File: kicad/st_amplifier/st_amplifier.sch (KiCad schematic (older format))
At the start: 67 parts

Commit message: He completed the first version of the board st_amplifier.
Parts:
- R1: value 2 к +/-0.5% -> 2 к +/-0.5%
- R2: value 28.7 к +/-0.5% -> 28.7 к +/-0.5%
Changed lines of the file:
@@
 Sheet 1 1
 Title ""
-Date "22 may 2015"
+Date "27 may 2015"
 Rev ""
 Comp ""
@@
 P 9300 3100
 F 0 "R1" H 9450 3350 71  0000 C CNN
-F 1 "2 к  +/-0.5%" H 9450 3250 71  0000 C CNN
+F 1 "2 к +/-0.5%" H 9450 3250 71  0000 C CNN
 F 2 "" H 9300 3100 60  0001 C CNN
 F 3 "" H 9300 3100 60  0001 C CNN
@@
 P 10500 3100
 F 0 "R2" H 10650 3350 71  0000 C CNN
-F 1 "28.7 к  +/-0.5%" H 10650 3250 71  0000 C CNN
+F 1 "28.7 к +/-0.5%" H 10650 3250 71  0000 C CNN
 F 2 "" H 10500 3100 60  0001 C CNN
 F 3 "" H 10500 3100 60  0001 C CNN

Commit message: Adding new version st_amplifier.
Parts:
- added C35, C36: 22 п, symbol CAPITORS
- added R21, R22: 220, symbol RESISTOR
- added R25, R26: 4.7, symbol RESISTOR
- added XP3: WF-3, ~, symbol PIN_M_3
- C12, C13: value 10 п -> 22 п
- C21, C27: value 100 п -> 220 п
- C28, C9: value 0.1 мк -> 0.047 мк
- XP1: renamed from XS2; symbol PIN_F_5 -> PIN_M_5
- XP2: renamed from XS4; value WF-4 -> WF-3; symbol PIN_M_4 -> PIN_M_3
- renumbered XS3 to XS2, XS6 to XS3
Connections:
- wire segments 201 -> 204
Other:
- moved on the sheet: C20, C24, R12, R18, R19, R4

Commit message: New commit.
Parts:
- added C37, C38: 22 п, symbol CAPITORS
- R14, R2: value 28.7 к +/-0.5% -> 28 к +/-0.5%
- R6, R8: value 22.1 к +/-0.5% -> 24 к +/-0.5%
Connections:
- net +29V: now also XP1.1; no longer XP1.2
- net MU/ST: now also XP1.2; no longer XP1.1
- net at DA4.14 (OUT), L1.2, R2.2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: now also C38.2
- net at DA4.2 (~IN), R1.2, R2.1: now also C38.1
- net at DA5.14 (OUT), L2.2, R14.2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: now also C37.2
- net at DA5.2 (~IN), R13.2, R14.1: now also C37.1
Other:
- moved on the sheet: C24, C27, R18, R22, XP3
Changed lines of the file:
@@
 Sheet 1 1
 Title ""
-Date "27 may 2015"
+Date "4 jun 2015"
 Rev ""
 Comp ""
@@
 Wire Wire Line
 	2800 6100 3350 6100
-Wire Wire Line
-	3350 6100 3350 5950
 Connection ~ 2800 6100
 Wire Wire Line
@@
 Connection ~ 12400 5600
 Wire Wire Line
-	9850 3650 9750 3650
-Wire Wire Line
-	9750 3650 9750 3100
+	9750 3650 9850 3650
+Wire Wire Line
+	9750 2700 9750 3650
 Wire Wire Line
 	8800 3200 8800 3100
@@
 	8800 3550 9100 3550
 Wire Wire Line
-	11550 3100 11550 3650
+	11550 2700 11550 3650
 Wire Wire Line
 	9100 3450 9100 3750
@@
 U 1 1 532EE9DE
 P 9300 3100
-F 0 "R1" H 9450 3350 71  0000 C CNN
-F 1 "2 к +/-0.5%" H 9450 3250 71  0000 C CNN
+F 0 "R1" H 9350 3350 71  0000 C CNN
+F 1 "2 к +/-0.5%" H 9350 3250 71  0000 C CNN
 F 2 "" H 9300 3100 60  0001 C CNN
 F 3 "" H 9300 3100 60  0001 C CNN
@@
 P 10500 3100
 F 0 "R2" H 10650 3350 71  0000 C CNN
-F 1 "28.7 к +/-0.5%" H 10650 3250 71  0000 C CNN
+F 1 "28 к +/-0.5%" H 10650 3250 71  0000 C CNN
 F 2 "" H 10500 3100 60  0001 C CNN
 F 3 "" H 10500 3100 60  0001 C CNN
@@
 Connection ~ 12200 9150
 Wire Wire Line
-	9650 7200 9550 7200
-Wire Wire Line
-	9550 7200 9550 6650
+	9550 7200 9650 7200
+Wire Wire Line
+	9550 6200 9550 7200
 Wire Wire Line
 	8600 6750 8600 6650
@@
 	8600 7100 8900 7100
 Wire Wire Line
-	11350 6650 11350 7200
+	11350 6200 11350 7200
 Wire Wire Line
 	8900 7000 8900 7300
@@
 U 1 1 552A86A8
 P 9100 6650
-F 0 "R13" H 9250 6900 71  0000 C CNN
-F 1 "2 к +/-0.5%" H 9250 6800 71  0000 C CNN
+F 0 "R13" H 9150 6900 71  0000 C CNN
+F 1 "2 к +/-0.5%" H 9150 6800 71  0000 C CNN
 F 2 "" H 9100 6650 60  0001 C CNN
 F 3 "" H 9100 6650 60  0001 C CNN
@@
 P 10300 6650
 F 0 "R14" H 10450 6900 71  0000 C CNN
-F 1 "28.7 к +/-0.5%" H 10450 6800 71  0000 C CNN
+F 1 "28 к +/-0.5%" H 10450 6800 71  0000 C CNN
 F 2 "" H 10300 6650 60  0001 C CNN
 F 3 "" H 10300 6650 60  0001 C CNN
@@
 Text Label 6900 1350 2    60   ~ 0
 +15V
-Connection ~ 3350 6700
-Wire Wire Line
-	2550 6700 2950 6700
-Wire Wire Line
-	3200 6700 3850 6700
-Wire Wire Line
-	2800 7100 2800 7550
-Connection ~ 2800 6700
-Wire Wire Line
-	2800 6700 2800 6850
-Wire Wire Line
-	3350 6700 3350 6850
-Wire Wire Line
-	2800 7250 3350 7250
-Wire Wire Line
-	3350 7250 3350 7100
-Connection ~ 2800 7250
-Text Label 2800 7550 1    60   ~ 0
+Connection ~ 3350 6650
+Wire Wire Line
+	2550 6650 2950 6650
+Wire Wire Line
+	3200 6650 3950 6650
+Wire Wire Line
+	2800 7050 2800 7500
+Connection ~ 2800 6650
+Wire Wire Line
+	2800 6650 2800 6800
+Wire Wire Line
+	3350 6650 3350 6800
+Wire Wire Line
+	2800 7200 3350 7200
+Connection ~ 2800 7200
+Text Label 2800 7500 1    60   ~ 0
 GND
 $Comp
 L RESISTOR R18
 U 1 1 552A8EFC
-P 2800 7100
-F 0 "R18" V 3000 7300 71  0000 C CNN
-F 1 "22 к" V 2850 7300 71  0000 C CNN
-F 2 "" H 2800 7100 60  0001 C CNN
-F 3 "" H 2800 7100 60  0001 C CNN
-	1    2800 7100
+P 2800 7050
+F 0 "R18" V 3000 7250 71  0000 C CNN
+F 1 "22 к" V 2850 7250 71  0000 C CNN
+F 2 "" H 2800 7050 60  0001 C CNN
+F 3 "" H 2800 7050 60  0001 C CNN
+	1    2800 7050
 	0    -1   -1   0
 $EndComp
@@
 L CAPITORS C27
 U 1 1 552A8F02
-P 3350 7100
-F 0 "C27" V 3550 6850 71  0000 C CNN
-F 1 "220 п" V 3400 6800 71  0000 C CNN
-F 2 "" H 3350 7100 60  0001 C CNN
-F 3 "" H 3350 7100 60  0001 C CNN
-	1    3350 7100
+P 3350 7050
+F 0 "C27" V 3550 6800 71  0000 C CNN
+F 1 "220 п" V 3400 6750 71  0000 C CNN
+F 2 "" H 3350 7050 60  0001 C CNN
+F 3 "" H 3350 7050 60  0001 C CNN
+	1    3350 7050
 	0    -1   -1   0
 $EndComp
@@
 L CAPITORS C24
 U 1 1 552A8F08
-P 2300 6700
-F 0 "C24" H 2250 6850 71  0000 C CNN
-F 1 "2.2 мк" H 2600 6850 71  0000 C CNN
-F 2 "" H 2300 6700 60  0001 C CNN
-F 3 "" H 2300 6700 60  0001 C CNN
-	1    2300 6700
+P 2300 6650
+F 0 "C24" H 2250 6800 71  0000 C CNN
+F 1 "2.2 мк" H 2600 6800 71  0000 C CNN
+F 2 "" H 2300 6650 60  0001 C CNN
+F 3 "" H 2300 6650 60  0001 C CNN
+	1    2300 6650
 	1    0    0    -1
 $EndComp
@@
 GND
 Wire Wire Line
-	3850 6700 3850 5950
-Wire Wire Line
-	3850 5950 4850 5950
+	3950 6650 3950 5950
+Wire Wire Line
+	3950 5950 4850 5950
 $Comp
 L RESISTOR R8
@@
 P 6100 5150
 F 0 "R8" H 6750 5250 71  0000 C CNN
-F 1 "22.1 к +/-0.5%" H 7050 5100 71  0000 C CNN
+F 1 "24 к +/-0.5%" H 7050 5100 71  0000 C CNN
 F 2 "" H 6100 5150 60  0001 C CNN
 F 3 "" H 6100 5150 60  0001 C CNN
@@
 P 4850 4750
 F 0 "R6" H 4950 4600 71  0000 C CNN
-F 1 "22.1 к +/-0.5%" H 5250 4450 71  0000 C CNN
+F 1 "24 к +/-0.5%" H 5250 4450 71  0000 C CNN
 F 2 "" H 4850 4750 60  0001 C CNN
 F 3 "" H 4850 4750 60  0001 C CNN
@@
 Wire Wire Line
 	2050 2300 2450 2300
-Text Label 2450 2300 2    60   ~ 0
+Text Label 2450 2400 2    60   ~ 0
 MU/ST
 $Comp
@@
 Wire Wire Line
 	2050 2400 2450 2400
-Text Label 2450 2400 2    60   ~ 0
+Text Label 2450 2300 2    60   ~ 0
 +29V
 Wire Wire Line
@@
 L PIN_M_3 XP3
 U 1 1 55656B81
-P 1900 6700
-F 0 "XP3" H 2000 6900 50  0000 L BNN
-F 1 "WF-3" H 1950 6800 50  0000 L BNN
-F 2 "~" H 2350 6850 50  0001 C CNN
-F 3 "" H 1900 6700 60  0001 C CNN
-	1    1900 6700
+P 1900 6650
+F 0 "XP3" H 2000 6850 50  0000 L BNN
+F 1 "WF-3" H 1950 6750 50  0000 L BNN
+F 2 "~" H 2350 6800 50  0001 C CNN
+F 3 "" H 1900 6650 60  0001 C CNN
+	1    1900 6650
 	-1   0    0    -1
 $EndComp
@@
 	1950 5550 2300 5550
 Wire Wire Line
-	2300 6700 1900 6700
-Text Label 2250 6900 2    60   ~ 0
+	2300 6650 1900 6650
+Text Label 2250 6850 2    60   ~ 0
 GND
 Wire Wire Line
 	1950 5750 2250 5750
 Wire Wire Line
-	2250 6900 1900 6900
+	2250 6850 1900 6850
 $Comp
 L RESISTOR R25
@@
 L RESISTOR R22
 U 1 1 5565738B
-P 2950 6700
-F 0 "R22" H 3100 6900 71  0000 C CNN
-F 1 "220" H 3100 6800 71  0000 C CNN
-F 2 "" H 2950 6700 60  0001 C CNN
-F 3 "" H 2950 6700 60  0001 C CNN
-	1    2950 6700
+P 2950 6650
+F 0 "R22" H 3100 6850 71  0000 C CNN
+F 1 "220" H 3100 6750 71  0000 C CNN
+F 2 "" H 2950 6650 60  0001 C CNN
+F 3 "" H 2950 6650 60  0001 C CNN
+	1    2950 6650
 	1    0    0    -1
 $EndComp
@@
 Wire Wire Line
 	3200 5550 4850 5550
+Wire Wire Line
+	3350 7200 3350 7050
+Wire Wire Line
+	3350 6100 3350 5950
+$Comp
+L CAPITORS C38
+U 1 1 55706D76
+P 10500 2700
+F 0 "C38" H 10650 3000 71  0000 C CNN
+F 1 "22 п" H 10600 2850 71  0000 C CNN
+F 2 "" H 10500 2700 60  0001 C CNN
+F 3 "" H 10500 2700 60  0001 C CNN
+	1    10500 2700
+	1    0    0    -1
+$EndComp
+Wire Wire Line
+	10750 2700 11550 2700
+Connection ~ 11550 3100
+Wire Wire Line
+	9750 2700 10500 2700
+$Comp
+L CAPITORS C37
+U 1 1 55706FB2
+P 10300 6200
+F 0 "C37" H 10450 6500 71  0000 C CNN
+F 1 "22 п" H 10400 6350 71  0000 C CNN
+F 2 "" H 10300 6200 60  0001 C CNN
+F 3 "" H 10300 6200 60  0001 C CNN
+	1    10300 6200
+	1    0    0    -1
+$EndComp
+Wire Wire Line
+	9550 6200 10300 6200
+Wire Wire Line
+	10550 6200 11350 6200
+Connection ~ 11350 6650
 $EndSCHEMATC

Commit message: Corrected power amplifier circuit (st_amplifier).
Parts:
- C28, C9: value 0.047 мк -> 0.1 мк
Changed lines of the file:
@@
 Sheet 1 1
 Title ""
-Date "4 jun 2015"
+Date "22 nov 2015"
 Rev ""
 Comp ""
@@
 P 13600 3750
 F 0 "C9" V 13700 4050 71  0000 C CNN
-F 1 "0.047 мк" V 13800 4100 71  0000 C CNN
+F 1 "0.1 мк" V 13800 4100 71  0000 C CNN
 F 2 "" H 13600 3750 60  0001 C CNN
 F 3 "" H 13600 3750 60  0001 C CNN
@@
 U 1 1 532EEF8D
 P 13600 4100
-F 0 "R5" V 13650 4300 71  0000 C CNN
-F 1 "10" V 13750 4300 71  0000 C CNN
+F 0 "R5" V 13650 4400 71  0000 C CNN
+F 1 "10" V 13750 4400 71  0000 C CNN
 F 2 "" H 13600 4100 60  0001 C CNN
 F 3 "" H 13600 4100 60  0001 C CNN
@@
 P 13400 7300
 F 0 "C28" V 13500 7600 71  0000 C CNN
-F 1 "0.047 мк" V 13600 7650 71  0000 C CNN
+F 1 "0.1 мк" V 13600 7600 71  0000 C CNN
 F 2 "" H 13400 7300 60  0001 C CNN
 F 3 "" H 13400 7300 60  0001 C CNN
@@
 U 1 1 552A8676
 P 13400 7650
-F 0 "R20" V 13450 7850 71  0000 C CNN
-F 1 "10" V 13550 7850 71  0000 C CNN
+F 0 "R20" V 13450 7950 71  0000 C CNN
+F 1 "10" V 13550 7950 71  0000 C CNN
 F 2 "" H 13400 7650 60  0001 C CNN
 F 3 "" H 13400 7650 60  0001 C CNN

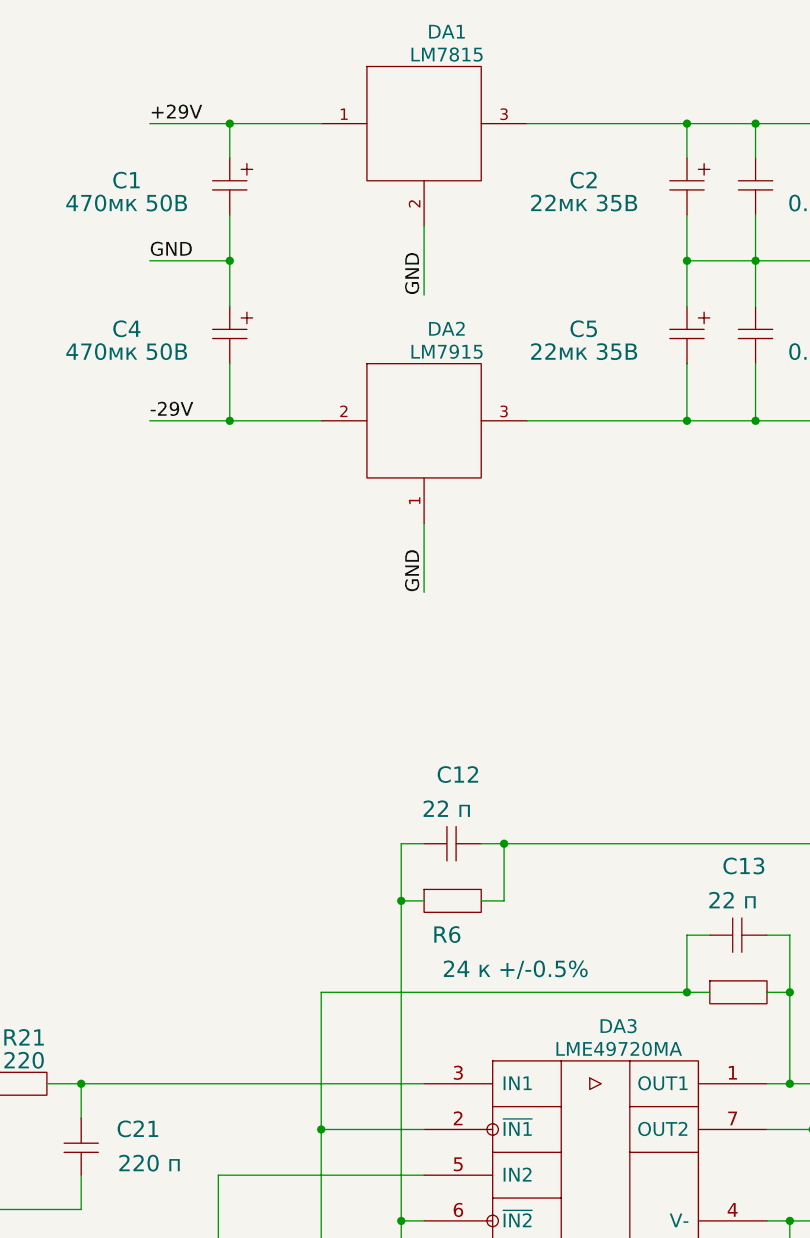
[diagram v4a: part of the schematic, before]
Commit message: Moved to kicad 4.0.0
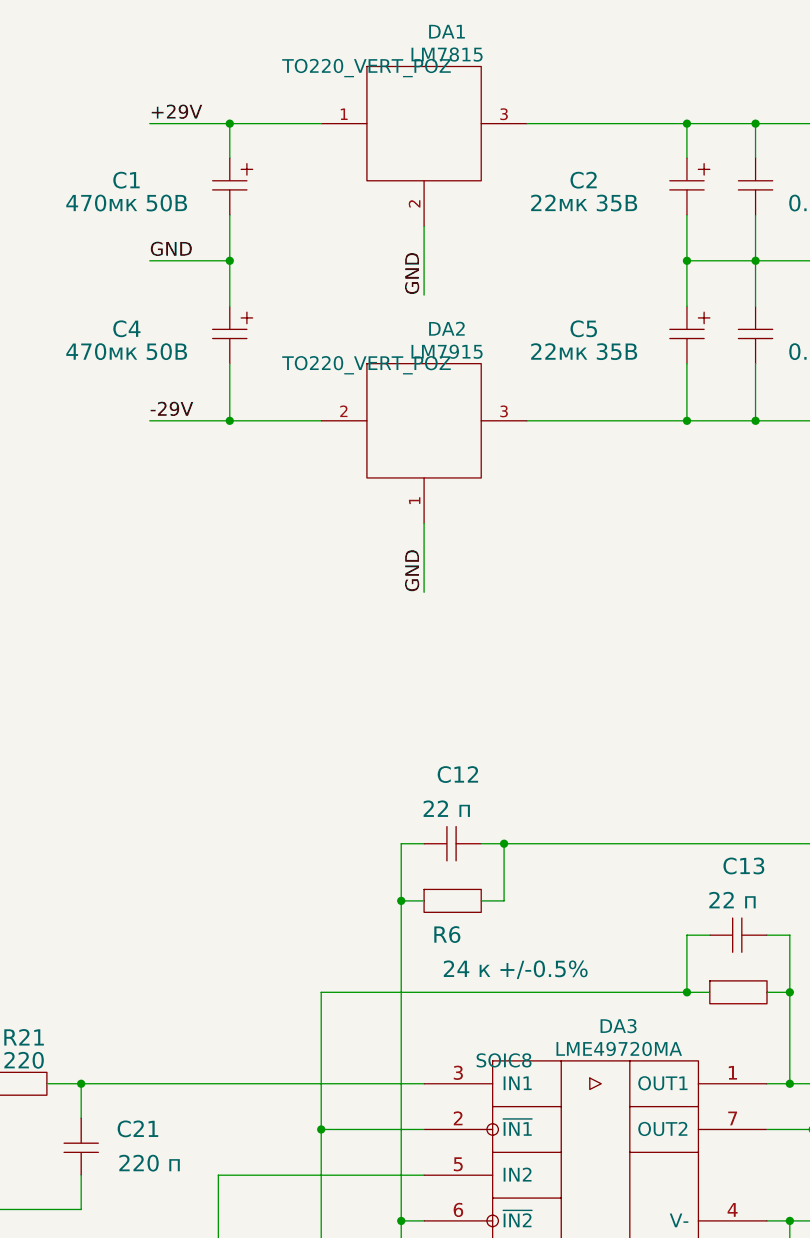
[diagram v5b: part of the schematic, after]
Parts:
- C1, C4: footprint (none) -> LFcomponents:CAPACITOR_CD263_5.08_D10
- C10, C15, C17, C29, C32, C34: footprint (none) -> LFcomponents:CAPACITOR_CBB21_15_16x6
- C11, C25, C30, C7: footprint (none) -> LFcomponents:CAPACITOR_5.08_D13
- C12, C13, C21, C22, C23, C27, C3, C35, C36, C37, C38, C6, R10, R11, R12, R15, R16, R18, R19, R21, R22, R25, R26, R4, R6, R7, R8, R9: footprint (none) -> LFsmd_case:SMD0805
- C14, C16, C31, C33: footprint (none) -> LFcomponents:CAPACITOR_10_D22
- C18, C19: footprint (none) -> LFcomponents:CAPACITOR_0511
- C2, C5: footprint (none) -> LFcomponents:CAPACITOR_CD263_2.54_D6.3
- C20, C24, C26, C8: footprint (none) -> LFcomponents:CAPACITOR_CBB21_20_24x11
- C28, C9: footprint (none) -> LFcomponents:CAPACITOR_CBB21_10_12x6
- DA1, DA2: footprint ~ -> TO220_VERT_POZ~
- DA3: footprint ~ -> SOIC8~
- DA4, DA5: footprint (none) -> LFcomponents:MULTIWATT15
- L1, L2: footprint (none) -> LFcomponents:INDUCTORS_1_15x8
- R1, R13, R14, R2: footprint (none) -> LFsmd_case:SMD1206
- R17, R20, R3, R5: footprint (none) -> LFcomponents:RESISTOR_2W
- VD1: footprint (none) -> LFcomponents:DO-41
- XP1: footprint ~ -> WF-5~
- XP2, XP3: footprint ~ -> WF-3~
- XS1: footprint ~ -> DG126-5.0-03P-14~
- XS2, XS3: footprint ~ -> DG126-5.0-02P-14~

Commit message: Поправил st_amplifier для новой версии kicad.
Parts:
- C1, C11, C14, C16, C18, C19, C2, C25, C30, C31, C33, C4, C5, C7: symbol CAPITORS_ELECTROLYTIC -> LFcapitors:CAPITORS_ELECTROLYTIC
- C10, C12, C13, C15, C17, C20, C21, C22, C24, C26, C27, C28, C29, C3, C32, C34, C35, C36, C37, C38, C6, C8, C9: symbol CAPITORS -> LFcapitors:CAPITORS
- C23: symbol CAPITORS -> LFresistor:RESISTOR
- DA1: footprint TO220_VERT_POZ~ -> ~; symbol 7815 -> LFcomponents:7815
- DA2: footprint TO220_VERT_POZ~ -> ~; symbol 7915 -> LFcomponents:7915
- DA3: footprint SOIC8~ -> ~; symbol LM258 -> LFcomponents:LM258
- DA4, DA5: symbol TDA7293 -> LFcomponents:TDA7293
- L1, L2: symbol INDUCTOR_3 -> LFtransformator:INDUCTOR_3
- R1, R10, R11, R12, R13, R14, R15, R16, R18, R19, R2, R21, R22, R25, R26, R4, R6, R7, R8, R9: symbol RESISTOR -> LFresistor:RESISTOR
- R17, R20, R3, R5: symbol RESISTOR_2W -> LFresistor:RESISTOR_2W
- VD1: symbol DIODE -> LFdiod:DIODE
- XP1: symbol PIN_M_5 -> LFconnectors:connector_5pin_gost
- XP2, XP3: symbol PIN_M_3 -> LFconnectors:connector_3pin_gost
- XS1: symbol PIN_F_3 -> LFconnectors:connector_3pin_gost
- XS2, XS3: symbol PIN_F_2 -> LFconnectors:connector_2pin_gost
